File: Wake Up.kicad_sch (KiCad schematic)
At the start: 14 parts, among them Q28 ZXMP10A13F, SW8 Push_Button

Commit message: worked on MCU
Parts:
- renumbered C56 to C19, C59 to C20, D52 to D23, D53 to D24, D55 to D25, D56 to D26, Q28 to Q10, R150 to R48, R152 to R49, R156 to R50, R161 to R51, R162 to R52, R164 to R53, SW8 to SW3
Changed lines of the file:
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@@
 		(on_board yes)
 		(dnp no)
-		(property "Reference" "D53"
+		(property "Reference" "D24"
 			(at 138.684 102.87 0)
 			(effects
@@
 			(project "Project-Star"
 				(path "/fc8533bc-25dd-4c20-9b4c-ffebebd6739b/e8da5d81-614b-4fe5-84b3-4c351fab7114/9d9414eb-0fa9-444a-a653-4c48988997ba"
-					(reference "D53")
+					(reference "D24")
 					(unit 1)
 				)
@@
 		(on_board yes)
 		(dnp no)
-		(property "Reference" "R161"
+		(property "Reference" "R51"
 			(at 158.496 94.234 0)
 			(effects
@@
 			(project "Project-Star"
 				(path "/fc8533bc-25dd-4c20-9b4c-ffebebd6739b/e8da5d81-614b-4fe5-84b3-4c351fab7114/9d9414eb-0fa9-444a-a653-4c48988997ba"
-					(reference "R161")
+					(reference "R51")
 					(unit 1)
 				)
@@
 		(on_board yes)
 		(dnp no)
-		(property "Reference" "R162"
+		(property "Reference" "R52"
 			(at 158.496 105.664 0)
 			(effects
@@
 			(project "Project-Star"
 				(path "/fc8533bc-25dd-4c20-9b4c-ffebebd6739b/e8da5d81-614b-4fe5-84b3-4c351fab7114/9d9414eb-0fa9-444a-a653-4c48988997ba"
-					(reference "R162")
+					(reference "R52")
 					(unit 1)
 				)
@@
 		(on_board yes)
 		(dnp no)
-		(property "Reference" "R164"
+		(property "Reference" "R53"
 			(at 156.21 87.884 90)
 			(effects
@@
 			(project "Project-Star"
 				(path "/fc8533bc-25dd-4c20-9b4c-ffebebd6739b/e8da5d81-614b-4fe5-84b3-4c351fab7114/9d9414eb-0fa9-444a-a653-4c48988997ba"
-					(reference "R164")
+					(reference "R53")
 					(unit 1)
 				)
@@
 		(on_board yes)
 		(dnp no)
-		(property "Reference" "D52"
+		(property "Reference" "D23"
 			(at 127 76.454 90)
 			(effects
@@
 			(project "Project-Star"
 				(path "/fc8533bc-25dd-4c20-9b4c-ffebebd6739b/e8da5d81-614b-4fe5-84b3-4c351fab7114/9d9414eb-0fa9-444a-a653-4c48988997ba"
-					(reference "D52")
+					(reference "D23")
 					(unit 1)
 				)
@@
 		(on_board yes)
 		(dnp no)
-		(property "Reference" "D56"
+		(property "Reference" "D26"
 			(at 166.624 102.87 0)
 			(effects
@@
 			(project "Project-Star"
 				(path "/fc8533bc-25dd-4c20-9b4c-ffebebd6739b/e8da5d81-614b-4fe5-84b3-4c351fab7114/9d9414eb-0fa9-444a-a653-4c48988997ba"
-					(reference "D56")
+					(reference "D26")
 					(unit 1)
 				)
@@
 		(on_board yes)
 		(dnp no)
-		(property "Reference" "R156"
+		(property "Reference" "R50"
 			(at 137.414 92.71 90)
 			(effects
@@
 			(project "Project-Star"
 				(path "/fc8533bc-25dd-4c20-9b4c-ffebebd6739b/e8da5d81-614b-4fe5-84b3-4c351fab7114/9d9414eb-0fa9-444a-a653-4c48988997ba"
-					(reference "R156")
+					(reference "R50")
 					(unit 1)
 				)
@@
 		(on_board yes)
 		(dnp no)
-		(property "Reference" "SW8"
+		(property "Reference" "SW3"
 			(at 172.466 90.424 0)
 			(effects
@@
 			(project "Project-Star"
 				(path "/fc8533bc-25dd-4c20-9b4c-ffebebd6739b/e8da5d81-614b-4fe5-84b3-4c351fab7114/9d9414eb-0fa9-444a-a653-4c48988997ba"
-					(reference "SW8")
+					(reference "SW3")
 					(unit 1)
 				)
@@
 		(on_board yes)
 		(dnp no)
-		(property "Reference" "R150"
+		(property "Reference" "R48"
 			(at 121.666 75.184 0)
 			(effects
@@
 			(project "Project-Star"
 				(path "/fc8533bc-25dd-4c20-9b4c-ffebebd6739b/e8da5d81-614b-4fe5-84b3-4c351fab7114/9d9414eb-0fa9-444a-a653-4c48988997ba"
-					(reference "R150")
+					(reference "R48")
 					(unit 1)
 				)
@@
 		(on_board yes)
 		(dnp no)
-		(property "Reference" "D55"
+		(property "Reference" "D25"
 			(at 163.83 106.934 90)
 			(effects
@@
 			(project "Project-Star"
 				(path "/fc8533bc-25dd-4c20-9b4c-ffebebd6739b/e8da5d81-614b-4fe5-84b3-4c351fab7114/9d9414eb-0fa9-444a-a653-4c48988997ba"
-					(reference "D55")
+					(reference "D25")
 					(unit 1)
 				)
@@
 		(on_board yes)
 		(dnp no)
-		(property "Reference" "R152"
+		(property "Reference" "R49"
 			(at 124.714 102.87 90)
 			(effects
@@
 			(project "Project-Star"
 				(path "/fc8533bc-25dd-4c20-9b4c-ffebebd6739b/e8da5d81-614b-4fe5-84b3-4c351fab7114/9d9414eb-0fa9-444a-a653-4c48988997ba"
-					(reference "R152")
+					(reference "R49")
 					(unit 1)
 				)
@@
 		(on_board yes)
 		(dnp no)
-		(property "Reference" "Q28"
+		(property "Reference" "Q10"
 			(at 134.62 81.788 0)
 			(effects
@@
 			(project "Project-Star"
 				(path "/fc8533bc-25dd-4c20-9b4c-ffebebd6739b/e8da5d81-614b-4fe5-84b3-4c351fab7114/9d9414eb-0fa9-444a-a653-4c48988997ba"
-					(reference "Q28")
+					(reference "Q10")
 					(unit 1)
 				)
@@
 		(on_board yes)
 		(dnp no)
-		(property "Reference" "C56"
+		(property "Reference" "C19"
 			(at 119.888 86.868 0)
 			(effects
@@
 			(project "Project-Star"
 				(path "/fc8533bc-25dd-4c20-9b4c-ffebebd6739b/e8da5d81-614b-4fe5-84b3-4c351fab7114/9d9414eb-0fa9-444a-a653-4c48988997ba"
-					(reference "C56")
+					(reference "C19")
 					(unit 1)
 				)
@@
 		(on_board yes)
 		(dnp no)
-		(property "Reference" "C59"
+		(property "Reference" "C20"
 			(at 137.414 97.79 90)
 			(effects
@@
 			(project "Project-Star"
 				(path "/fc8533bc-25dd-4c20-9b4c-ffebebd6739b/e8da5d81-614b-4fe5-84b3-4c351fab7114/9d9414eb-0fa9-444a-a653-4c48988997ba"
-					(reference "C59")
-					(unit 1)
-				)
+					(reference "C20")
+					(unit 1)
+				)

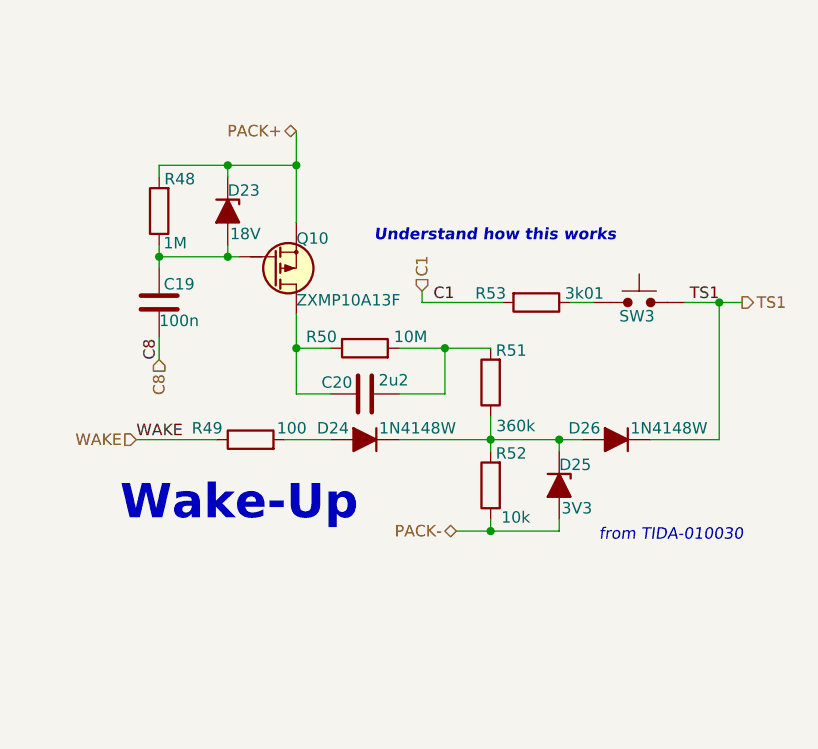
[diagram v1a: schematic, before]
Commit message: Added Fuel/Gas Guage
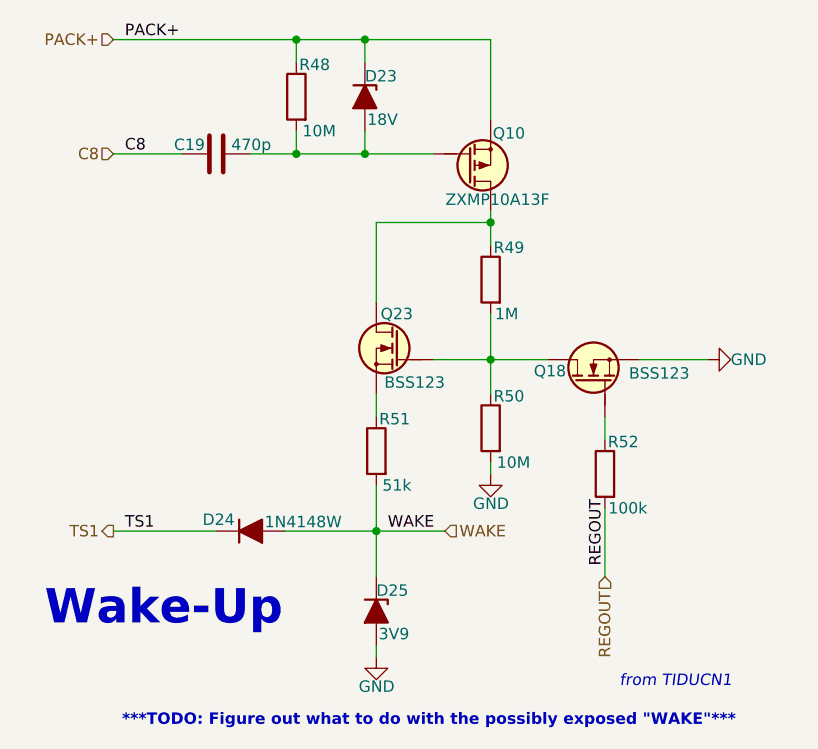
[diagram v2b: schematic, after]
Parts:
- removed C20: 2u2, symbol Device:C
- removed D26: 1N4148W, PCM_Diode_SMD_AKL:D_SOD-123, symbol PCM_Diode_AKL:1N4148W
- removed R53: 3k01, symbol Device:R
- removed SW3: Push_Button, Button_Switch_THT:SW_PUSH_6mm, symbol PCM_SL_Devices:Push_Button
- added Q18, Q23: BSS123, PCM_Package_TO_SOT_SMD_AKL:SOT-23, symbol PCM_Transistor_MOSFET_AKL:BSS123
- C19: value 100n -> 470p
- D25: value 3V3 -> 3V9
- R48: value 1M -> 10M
- R49: value 100 -> 1M
- R51: value 360k -> 51k
- R52: value 10k -> 100k
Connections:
- net C8: now also C19.1; no longer C19.2
- net PACK+: now also R48.1; no longer R48.2
- net TS1: now also D24.1 (K)
- net WAKE: now also D24.2 (A), D25.1 (K), R51.2; no longer R49.1
- net at R49.2: now also R50.1, Q18.3 (D), Q23.1 (G); no longer D24.2 (A)
- net GND: now reaches R50.2
- net GND: now also D25.2 (A), Q18.2 (S); no longer R51.2
- net at D23.2 (A), Q10.1 (G): now also C19.2, R48.2; no longer C19.1, R48.1
- net at Q10.3 (D): now also R49.1, Q23.3 (D); no longer R50.1
- net PACK-: no longer names the net of R52.1
- net PACK-: now also Q18.1 (G); no longer D25.2 (A)
- new net: Q23.2 (S), R51.1
- new net REGOUT: R52.2
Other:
- note added: "***TODO: Figure out what to do with the possibly exposed "WAKE"***"
- note added: "from TIDUCN1"
- note removed: "Understand how this works"
- note removed: "from TIDA-010030"
